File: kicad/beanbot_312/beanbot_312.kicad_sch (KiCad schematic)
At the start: 16 parts

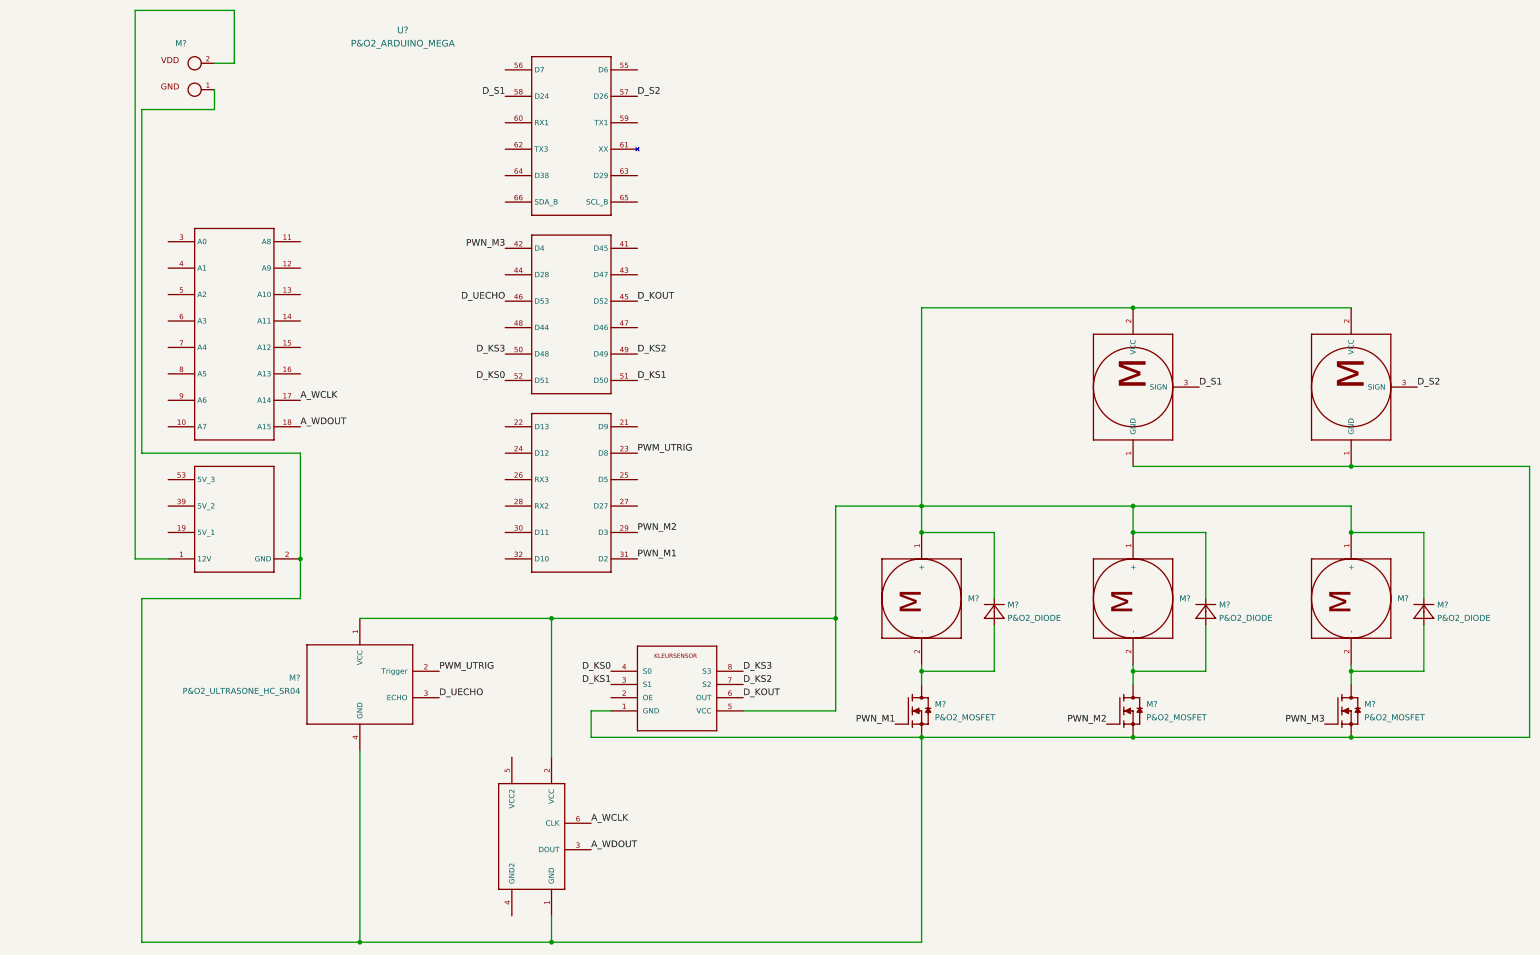
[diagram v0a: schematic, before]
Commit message: Some Progress to KiCad drawings (#8)
* Some Progress to KiCad drawings

* Some more progress to KiCad drawings

* Deleting wires and adding labels

Co-authored-by: Robin Martens <robin.martens@quivr.be>
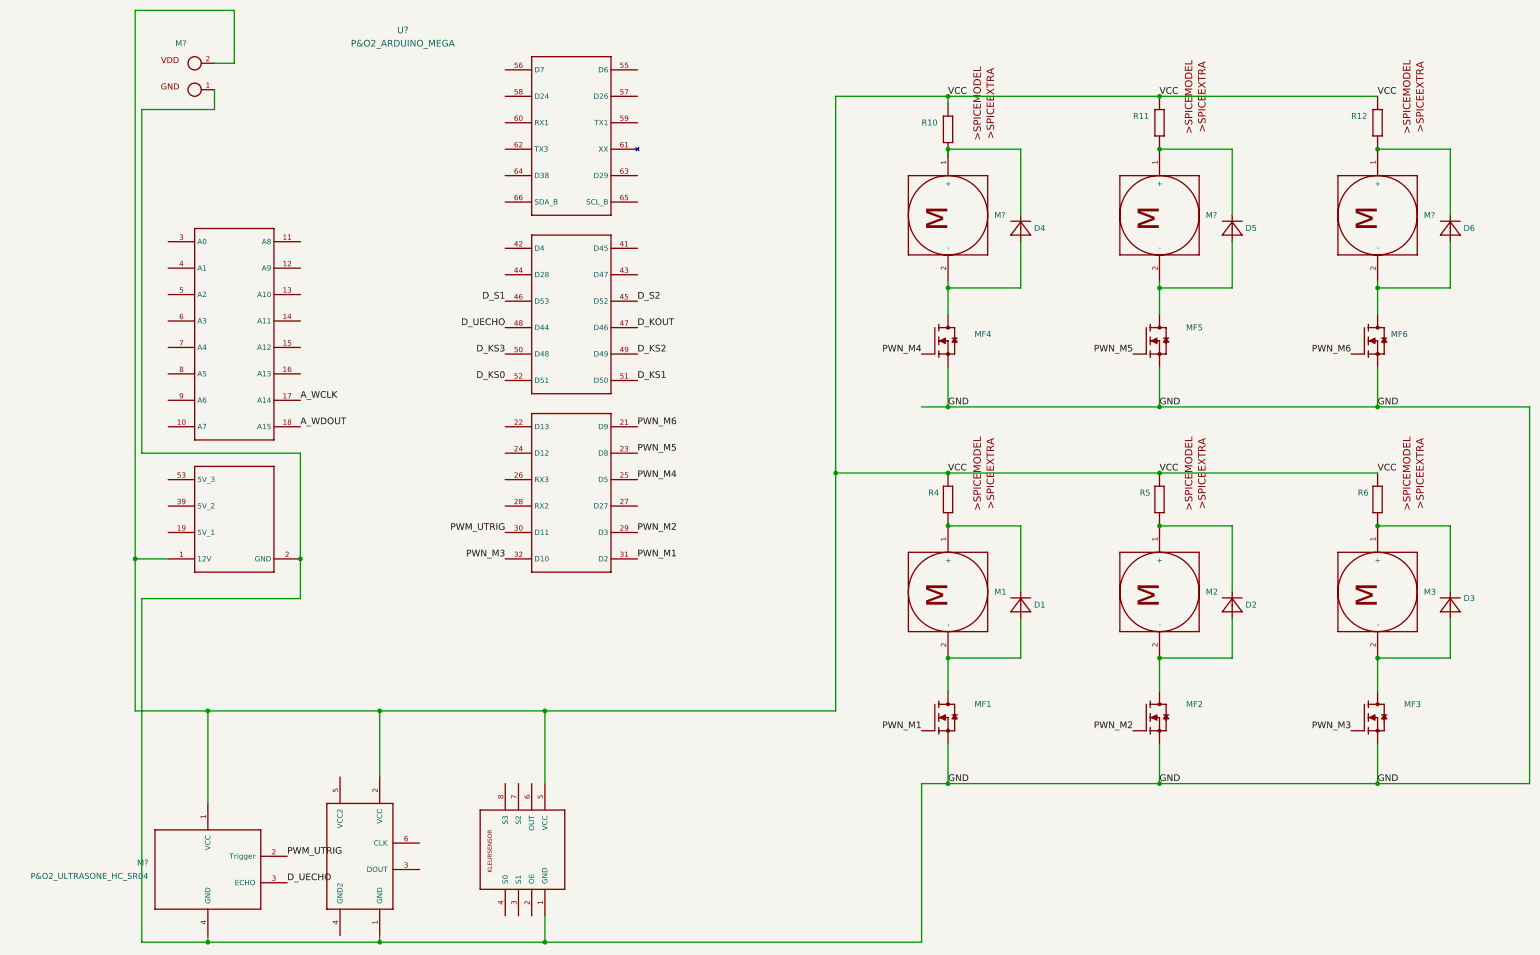
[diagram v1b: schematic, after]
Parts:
- removed M? (x3): P&O2_DC-MOTOR, P&O2_lib_MKDSN1_5_2-5_08, symbol 1_P&O2_lib:P&O2_DC-MOTOR
- removed M? (x3): P&O2_MOSFET, P&O2_lib_TO220V, symbol 1_P&O2_lib:P&O2_MOSFET
- removed M? (x3): P&O2_DIODE, P&O2_lib_D-12.5, symbol 1_P&O2_lib:P&O2_DIODE
- removed M? (x2): P&O2_SERVOMOTOR, P&O2_lib_SERVO-3PIN, symbol 1_P&O2_lib:P&O2_SERVOMOTOR
- added D1, D2, D3, D4, D5, D6: P&O2_DIODE, P&O2_lib_D-12.5, symbol 1_P&O2_lib:P&O2_DIODE
- added M1, M2, M3, M? (x3): P&O2_DC-MOTOR, P&O2_lib_MKDSN1_5_2-5_08, symbol 1_P&O2_lib:P&O2_DC-MOTOR
- added MF1, MF2, MF4, MF5, MF6: P&O2_MOSFET, P&O2_lib_TO220V, symbol 1_P&O2_lib:P&O2_MOSFET
- added MF3: \, P&O2_lib_TO220V, symbol 1_P&O2_lib:P&O2_MOSFET
- added R10, R11, R12, R4, R5, R6: P&O2_RESISTOR, P&O2_lib_0411_15, symbol 1_P&O2_lib:P&O2_RESISTOR
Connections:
- net A_WCLK: no longer M?.6 (CLK)
- net A_WDOUT: no longer M?.3 (DOUT)
- net D_KOUT: now also U?.47 (D46); no longer M?.6 (OUT), U?.45 (D52)
- net D_KS0: no longer M?.4 (S0)
- net D_KS1: no longer M?.3 (S1)
- net D_KS2: no longer M?.7 (S2)
- net D_KS3: no longer M?.8 (S3)
- net D_S1: now also U?.46 (D53); no longer U?.58 (D24)
- net D_S2: now also U?.45 (D52); no longer U?.57 (D26)
- net D_UECHO: now also U?.48 (D44); no longer U?.46 (D53)
- net PWM_UTRIG: now also U?.30 (D11); no longer U?.23 (D8)
- net PWN_M1: now also MF1.1 (eG)
- net PWN_M2: now also MF2.1 (eG)
- net PWN_M3: now also U?.32 (D10), MF3.1 (eG); no longer U?.42 (D4)
- net GND: now reaches M?.1 (GND), M?.1 (GND), M?.1 (GND), M?.4 (GND), U?.2 (GND)
- net GND: now also MF1.3 (S), MF2.3 (S), MF3.3 (S), MF4.3 (S), MF5.3 (S), MF6.3 (S)
- net VCC: now reaches M?.1 (VCC), M?.2 (VCC), M?.5 (VCC)
- net VCC: now also M?.2 (VDD), U?.1 (12V), R10.2, R11.2, R12.2, R4.2, R5.2, R6.2
- net PWN_M6: now reaches U?.21 (D9)
- net PWN_M6: now also MF6.1 (eG)
- net PWN_M4: now reaches U?.25 (D5)
- net PWN_M4: now also MF4.1 (eG)
- new net: D1.C, M1.1 (+), R4.1
- new net: D2.C, M2.1 (+), R5.1
- new net: D2.A, M2.2 (-), MF2.2 (D)
- new net: D3.A, M3.2 (-), MF3.2 (D)
- new net: D3.C, M3.1 (+), R6.1
- new net: D1.A, M1.2 (-), MF1.2 (D)
- new net: D4.C, M?.1 (+), R10.1
- new net: D4.A, M?.2 (-), MF4.2 (D)
- new net: D6.A, M?.2 (-), MF6.2 (D)
- new net: D6.C, M?.1 (+), R12.1
- new net: D5.A, M?.2 (-), MF5.2 (D)
- new net: D5.C, M?.1 (+), R11.1
- new net PWN_M5: MF5.1 (eG), U?.23 (D8)
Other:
- moved on the sheet: M?

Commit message: Finished schematic
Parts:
- removed M1, M2, M3, M? (x3): P&O2_DC-MOTOR, P&O2_lib_MKDSN1_5_2-5_08, symbol 1_P&O2_lib:P&O2_DC-MOTOR
- removed MF1, MF2, MF4, MF5, MF6: P&O2_MOSFET, P&O2_lib_TO220V, symbol 1_P&O2_lib:P&O2_MOSFET
- removed MF3: \, P&O2_lib_TO220V, symbol 1_P&O2_lib:P&O2_MOSFET
- removed R10, R11, R12, R4, R5, R6: P&O2_RESISTOR, P&O2_lib_0411_15, symbol 1_P&O2_lib:P&O2_RESISTOR
- added M10, M12, M13, M15, M16, M17, M18, M19, M2, M21, M22, M24, M27, M30, M32, M34, M37, M4, M40, M42, M44, M47, M50, M52, M7: P&O2_MEETPUNT, 1_P&O2_lib:P&O2_MEETPUNT, symbol 1_P&O2_lib:P&O2_MEETPUNT
- added M23, M25, M26, M29, M3, M33, M35, M36, M39, M43, M45, M46, M49, M6, M8, M9: P&O2_RESISTOR, 1_P&O2_lib:P&O2_RES, symbol 1_P&O2_lib:P&O2_RESISTOR
- added M28, M31, M38, M41, M48, M51: P&O2_DC-MOTOR, 1_P&O2_lib:P&O2_2PIN-SCREW-5.08, symbol 1_P&O2_lib:P&O2_DC-MOTOR
- added M5: P&O2_RGB_LED, 1_P&O2_lib:P&O2_RGB_LED, symbol 1_P&O2_lib:P&O2_RGB_LED
- added M53, M54, M55, M56, M57, M58: P&O2_MOSFET, 1_P&O2_lib:P&O2_TO220, symbol 1_P&O2_lib:P&O2_MOSFET
- added U2: LCD-016N002L, Display:LCD-016N002L, symbol Display_Character:LCD-016N002L
- D1: renamed from D4; footprint P&O2_lib_D-12.5 -> 1_P&O2_lib:P&O2_DIODE
- D2: renamed from D1; footprint P&O2_lib_D-12.5 -> 1_P&O2_lib:P&O2_DIODE
- D3: renamed from D5; footprint P&O2_lib_D-12.5 -> 1_P&O2_lib:P&O2_DIODE
- D4: renamed from D2; footprint P&O2_lib_D-12.5 -> 1_P&O2_lib:P&O2_DIODE
- D5: renamed from D6; footprint P&O2_lib_D-12.5 -> 1_P&O2_lib:P&O2_DIODE
- D6: renamed from D3; footprint P&O2_lib_D-12.5 -> 1_P&O2_lib:P&O2_DIODE
- M1: renamed from M?; footprint P&O2_lib_MKDSN1_5_2-5_08 -> 1_P&O2_lib:P&O2_2PIN-SCREW-5.08
- M11: renamed from M?; footprint P&O2_lib_MA04-1 -> 1_P&O2_lib:P&O2_ULTRASONE
- M14: renamed from M?; footprint P&O2_lib_GEWICHTSENSOR-6PIN -> 1_P&O2_lib:P&O2_GEWICHTSENSOR-6PIN
- M20: renamed from M?; footprint P&O2_lib_KLRS_FP -> 1_P&O2_lib:P&O2_KLEURENSENSOR-8PIN
- U1: renamed from U?; footprint (none) -> 1_P&O2_lib:P&O2_ARDUINO_MEGA
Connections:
- net A_WCLK: now also M14.6 (CLK), U1.3 (A0), M15.1 (TP); no longer U1.17 (A14)
- net A_WDOUT: now also M14.3 (DOUT), U1.4 (A1), M16.1 (TP); no longer U1.18 (A15)
- net D_KOUT: now also M20.6 (OUT), M21.1 (TP)
- net D_KS2: now also M20.7 (S2), M19.1 (TP)
- net D_KS3: now also M20.8 (S3), M18.1 (TP)
- net D_UECHO: now also M13.1 (TP)
- net GND: now also M20.2 (OE), M20.4 (S0), M26.2, M29.2, M36.2, M39.2, M46.2, M49.2, M53.3 (S), M54.3 (S), M55.3 (S), M56.3 (S), M57.3 (S), M58.3 (S), U2.1 (VSS), U2.3 (VO), U2.5 (R/~{W}), U2.K1
- net PWM_UTRIG: now also U1.32 (D10), M12.1 (TP); no longer U1.30 (D11)
- net PWN_M1: now also M23.1
- net PWN_M2: now also M33.1
- net PWN_M3: now also U1.42 (D4), M43.1; no longer U1.32 (D10)
- net PWN_M4: now also M25.1
- net PWN_M5: now also U1.55 (D6), M35.1; no longer U1.23 (D8)
- net PWN_M6: now also U1.56 (D7), M45.1; no longer U1.21 (D9)
- net 12V: now reaches D2.C
- net 12V: now also D1.C, D3.C, D4.C, D5.C, D6.C, M1.2 (VDD), M22.1 (TP), M28.1 (B), M31.1 (B), M38.1 (B), M41.1 (B), M48.1 (B), M51.1 (B)
- net 5V: now reaches M20.3 (S1)
- net 5V: now also M11.1 (VCC), M14.2 (VCC), M20.5 (VCC), U1.19 (5V_1), M17.1 (TP), M2.1 (TP), M5.2 (VCC), M8.2, U2.2 (VDD)
- net at D4.A: now also M41.2 (A), M42.1 (TP), M56.2 (D)
- net at D6.A: now also M51.2 (A), M52.1 (TP), M58.2 (D)
- net at D2.A: now also M31.2 (A), M32.1 (TP), M54.2 (D)
- net at D1.A: now also M28.2 (A), M30.1 (TP), M53.2 (D)
- net at D5.A: now also M48.2 (A), M50.1 (TP), M57.2 (D)
- net PWM_LEDR: now reaches U1.22 (D13)
- net PWM_LEDR: now also M3.2, M4.1 (TP)
- net PWM_LEDG: now reaches U1.24 (D12)
- net PWM_LEDG: now also M6.2, M7.1 (TP)
- net D_LCDDB5: now reaches U1.27 (D27)
- net D_LCDDB5: now also U2.12 (DB5)
- net D_LCDDB6: now reaches U1.44 (D28)
- net D_LCDDB6: now also U2.13 (DB6)
- net D_LCDDB4: now reaches U1.57 (D26)
- net D_LCDDB4: now also U2.11 (DB4)
- net D_LCDDB7: now reaches U1.63 (D29)
- net D_LCDDB7: now also U2.14 (DB7)
- net at D3.A: now also M38.2 (A), M40.1 (TP), M55.2 (D)
- net VERBINDING_WEEGELEMENT: now reaches M14.4 (GND2)
- net VERBINDING_WEEGELEMENT: now also M14.5 (VCC2)
- net D_KS0: no longer names the net of U1.52 (D51)
- net D_S1: no longer names the net of U1.46 (D53)
- net D_S2: no longer names the net of U1.45 (D52)
- removed net VCC: M1.2 (VDD), M11.1 (VCC), M14.2 (VCC), M20.5 (VCC), U1.1 (12V)
- new net: M25.2, M27.1 (TP), M29.1, M54.1 (eG)
- new net: M23.2, M24.1 (TP), M26.1, M53.1 (eG)
- new net: M35.2, M37.1 (TP), M39.1, M56.1 (eG)
- new net: M33.2, M34.1 (TP), M36.1, M55.1 (eG)
- new net: M45.2, M47.1 (TP), M49.1, M58.1 (eG)
- new net: M8.1, U2.A1
- new net: M43.2, M44.1 (TP), M46.1, M57.1 (eG)
- new net: M5.3 (G), M6.1
- new net: M3.1, M5.1 (R)
- new net: M5.4 (B), M9.1
- new net D_LCDE: U1.21 (D9), U2.6 (E)
- new net D_LCDRS: U1.23 (D8), U2.4 (RS)
- new net PWM_LEDB: M10.1 (TP), M9.2, U1.30 (D11)
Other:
- note added: "A1 = LED+ K1 = LED-"
- moved on the sheet: D1, D2, D3, D4, D5, D6, M1, M11, U1

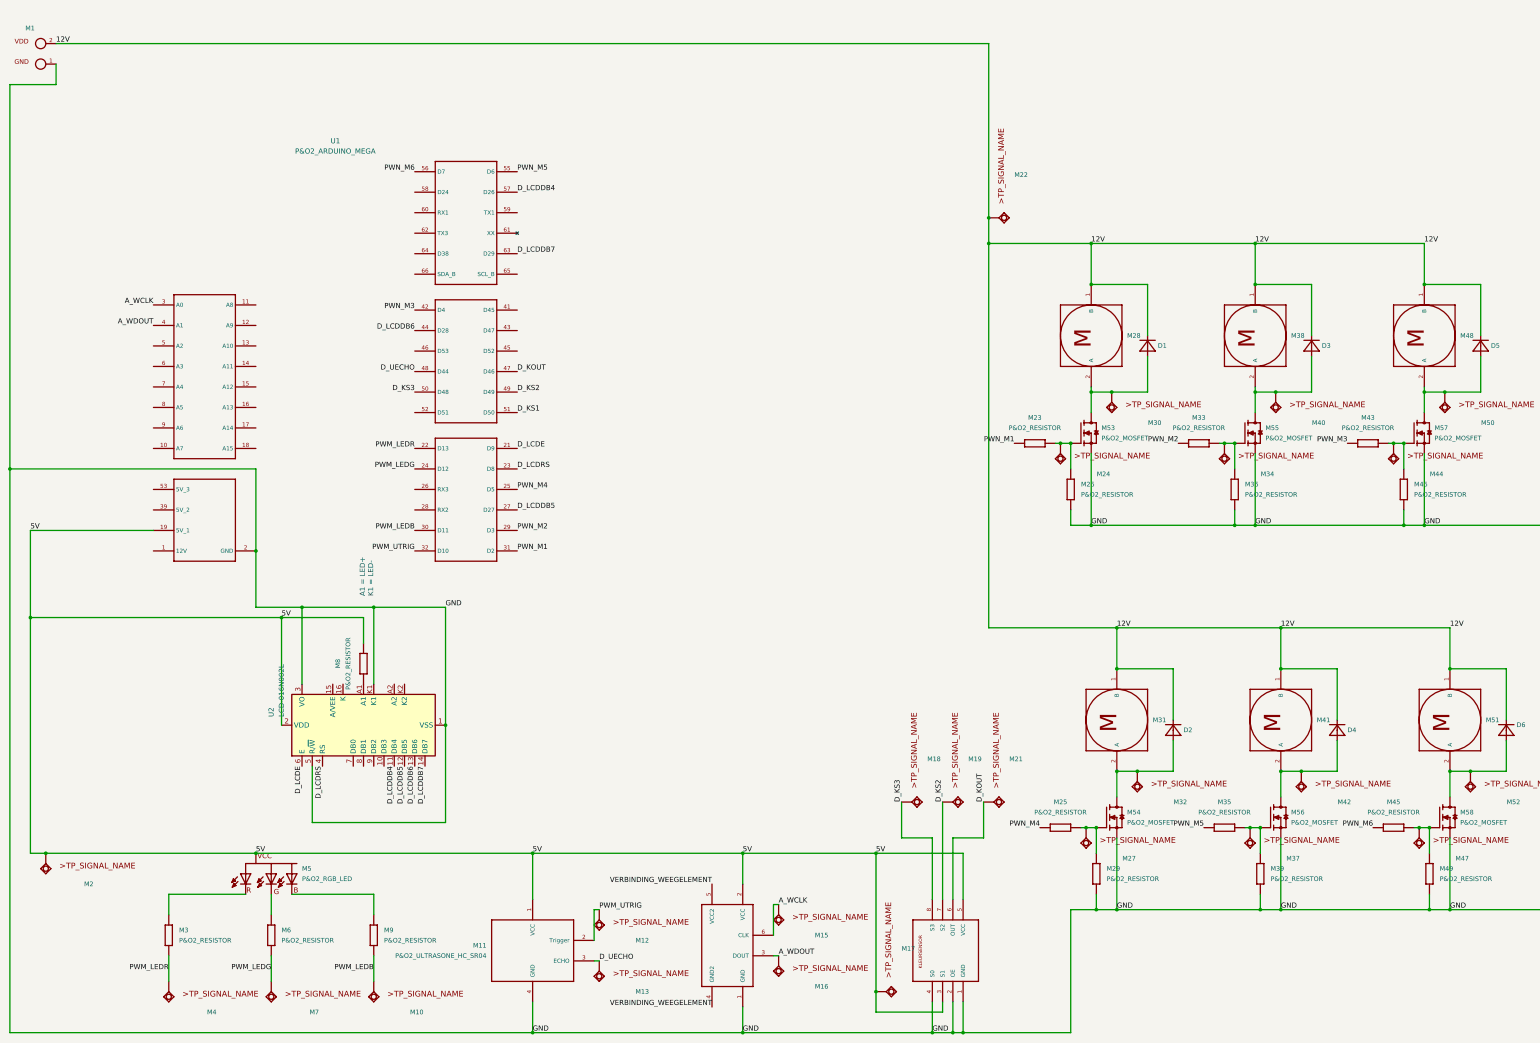
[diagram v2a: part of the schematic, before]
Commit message: Added IC to KiCad
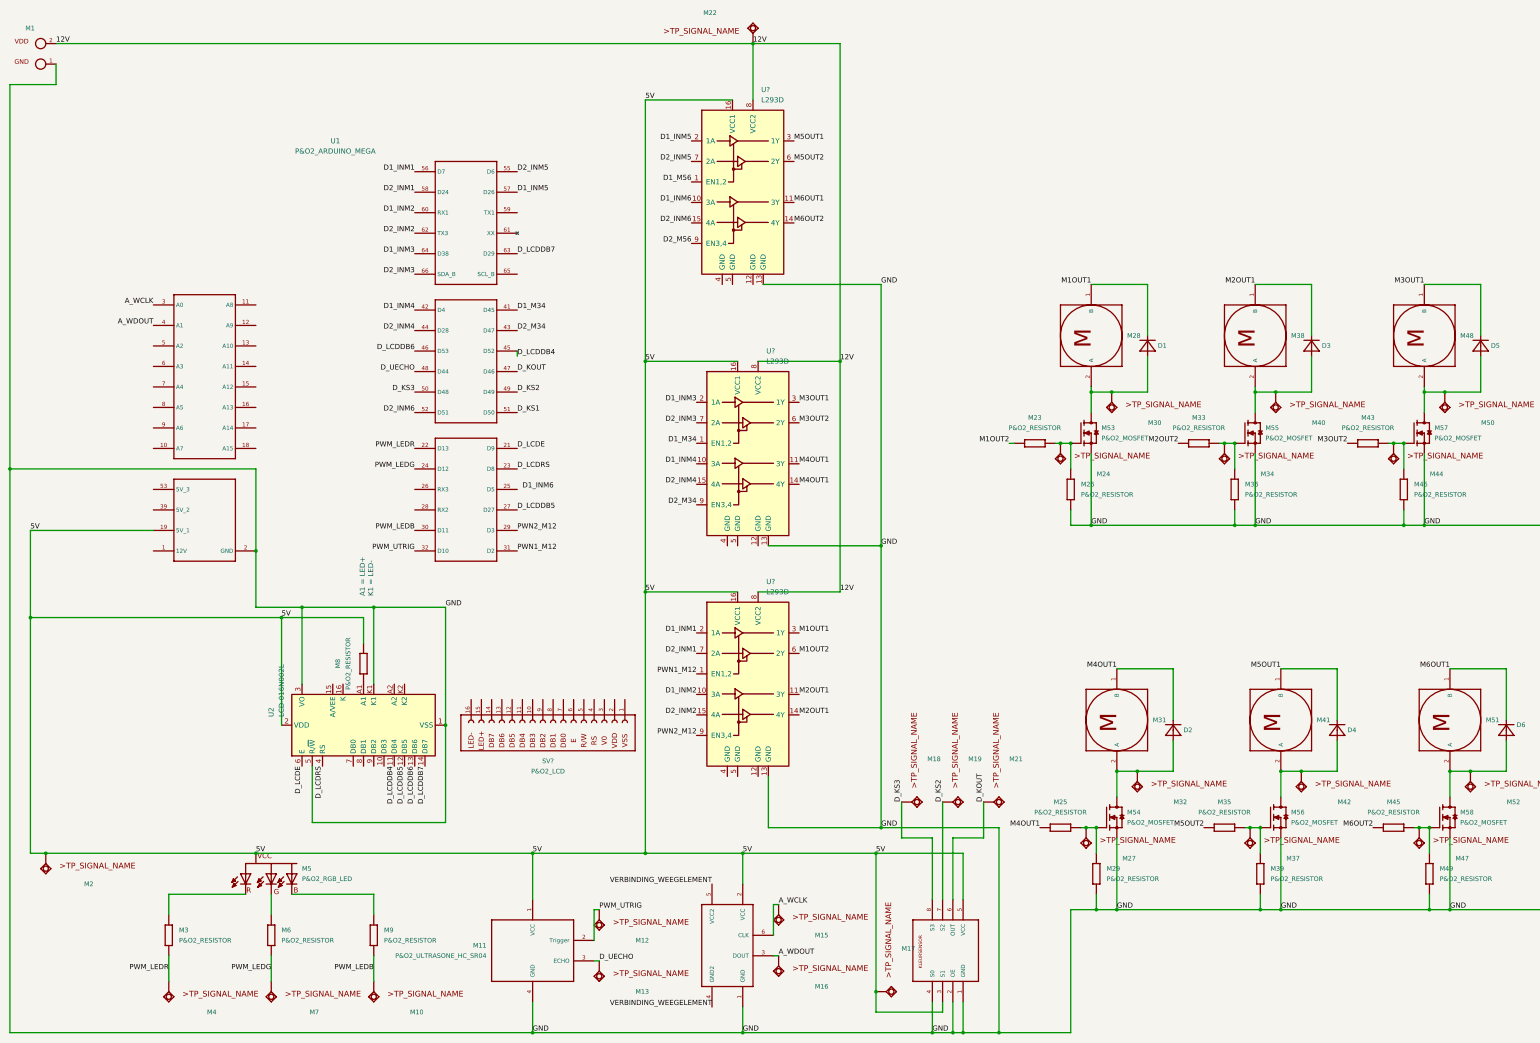
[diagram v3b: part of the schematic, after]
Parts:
- added SV?: P&O2_LCD, P&O2_lib_FE05-1, symbol 1_P&O2_lib:P&O2_LCD
- added U? (x3): L293D, Package_DIP:DIP-16_W7.62mm, symbol Driver_Motor:L293D
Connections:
- net 12V: now also U?.8 (VCC2), U?.8 (VCC2), U?.8 (VCC2); no longer D1.C, D2.C, D3.C, D4.C, D5.C, D6.C, M28.1 (B), M31.1 (B), M38.1 (B), M41.1 (B), M48.1 (B), M51.1 (B)
- net 5V: now also U?.16 (VCC1), U?.16 (VCC1), U?.16 (VCC1)
- net D_LCDDB4: now also U1.45 (D52); no longer U1.57 (D26)
- net D_LCDDB6: now also U1.46 (D53); no longer U1.44 (D28)
- net GND: now also U?.13 (GND), U?.13 (GND), U?.13 (GND)
- net D1_M34: now reaches U1.41 (D45)
- net D1_M34: now also U?.1 (EN1,2)
- net D2_M34: now reaches U1.43 (D47)
- net D2_M34: now also U?.9 (EN3,4)
- net D2_INM6: now reaches U1.52 (D51)
- net D2_INM6: now also U?.15 (4A)
- net D2_INM1: now reaches U1.58 (D24)
- net D2_INM1: now also U?.7 (2A)
- net D1_INM2: now reaches U1.60 (RX1)
- net D1_INM2: now also U?.10 (3A)
- net D2_INM2: now reaches U1.62 (TX3)
- net D2_INM2: now also U?.15 (4A)
- net D1_INM3: now reaches U1.64 (D38)
- net D1_INM3: now also U?.2 (1A)
- net D2_INM3: now reaches U1.66 (SDA_B)
- net D2_INM3: now also U?.7 (2A)
- net PWN_M1 renamed M1OUT2
- net M1OUT2: now also U?.6 (2Y); no longer U1.31 (D2)
- net PWN_M2 renamed M2OUT2
- net M2OUT2: no longer U1.29 (D3)
- net PWN_M3 renamed D1_INM4
- net D1_INM4: now also U?.10 (3A); no longer M43.1
- net PWN_M4: no longer names the net of U1.25 (D5)
- net PWN_M4: no longer M25.1
- net PWN_M5 renamed D2_INM5
- net D2_INM5: now also U?.7 (2A); no longer M35.1
- net PWN_M6 renamed D1_INM1
- net D1_INM1: now also U?.2 (1A); no longer M45.1
- new net D1_INM5: U1.57 (D26), U?.2 (1A)
- new net D1_INM6: U?.10 (3A)
- new net D1_M56: U?.1 (EN1,2)
- new net D2_INM4: U1.44 (D28), U?.15 (4A)
- new net D2_M56: U?.9 (EN3,4)
- new net M1OUT1: D1.C, M28.1 (B), U?.3 (1Y)
- new net M2OUT1: D3.C, M38.1 (B), U?.11 (3Y), U?.14 (4Y)
- new net M3OUT1: D5.C, M48.1 (B), U?.3 (1Y)
- new net M3OUT2: M43.1, U?.6 (2Y)
- new net M4OUT1: D2.C, M25.1, M31.1 (B), U?.11 (3Y), U?.14 (4Y)
- new net M5OUT1: D4.C, M41.1 (B), U?.3 (1Y)
- new net M5OUT2: M35.1, U?.6 (2Y)
- new net M6OUT1: D6.C, M51.1 (B), U?.11 (3Y)
- new net M6OUT2: M45.1, U?.14 (4Y)
- new net PWN1_M12: U1.31 (D2), U?.1 (EN1,2)
- new net PWN2_M12: U1.29 (D3), U?.9 (EN3,4)
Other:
- moved on the sheet: M22
